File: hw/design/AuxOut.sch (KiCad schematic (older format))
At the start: 41 parts

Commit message: aux output, documentation
finished aux output circuit, updated a lot of documentation, added datasheets
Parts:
- added TP?: GND, TestPoint:TestPoint_Keystone_5000-5004_Miniature, symbol Connector:TestPoint
- added TP? (x3): AUX_G, TestPoint:TestPoint_Keystone_5000-5004_Miniature, symbol Connector:TestPoint
- C?: VRating 50V -> 16V
- D?: value D_Schottky -> B130LAW-7-F; IRating (none) -> 1A; MfrNum (none) -> DiodesInc_B130LAW-7-F; VRating (none) -> 30V
- D?: footprint (none) -> Diode_SMD:D_SOD-123
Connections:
- net GND: now also TP?.1
- net GND1: now also TR?.6, TP?.1, TP?.1, TP?.1; no longer TR?.4
- net Fly_EN: now reaches R?.1, R?.2, U?.1 (EN/UVLO)
- net at D?.2 (A): now also TR?.4; no longer TR?.6
- net AuxIn renamed Vbus
- net AuxPOut renamed AuxOut_I
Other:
- moved on the sheet: C?, D?, R?, TP?

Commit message: reworked adjusters
new V/I adjustment scheme; modified LDO circuit to match
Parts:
- added C?: 4.7u, Capacitor_SMD:C_1206_3216Metric, symbol Device:C
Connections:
- net AuxOut_I: now also C?.1
- net GND1: now also C?.2
- no-connect marks 1 -> 2
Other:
- note added: "All resistors 0603 size unless otherwise stated\nAll capacitors 0603 size unless otherwise stated\nAll capacitors rated for 16V unless otherwise stated"
- note added: "Aux Output Indicator\n(Optional Circuit)"
- note removed: "Aux Output Indicator"
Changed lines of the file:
@@
 Connection ~ 9500 1850
 Wire Wire Line
-	9500 1850 9800 1850
+	9500 1850 10000 1850
 $Comp
 L power:GND1 #PWR?
@@
 Text Notes 6900 5450 0    50   ~ 0
 Slow On\nFast Off
-Text Notes 7200 3950 0    100  ~ 0
-Aux Output Indicator
+Text Notes 7050 3900 0    100  ~ 0
+Aux Output Indicator\n(Optional Circuit)
 Text Notes 10000 3000 0    50   ~ 0
 Triggers at 4.75V
@@
 Text Label 2650 2400 0    50   ~ 0
 Fly_EN
-Text HLabel 9800 1850 2    50   BiDi ~ 0
+Text HLabel 10350 1850 2    50   BiDi ~ 0
 AuxOut_I
 Text HLabel 1650 1700 0    50   BiDi ~ 0
@@
 	1    0    0    1
 $EndComp
+NoConn ~ 4550 2000
+$Comp
+L Device:C C?
+U 1 1 6038857F
+P 10000 2100
+F 0 "C?" H 10115 2191 50  0000 L CNN
+F 1 "4.7u" H 10115 2100 50  0000 L CNN
+F 2 "Capacitor_SMD:C_1206_3216Metric" H 10038 1950 50  0001 C CNN
+F 3 "~" H 10000 2100 50  0001 C CNN
+F 4 "Murata_GRM21BR71C475KE51L" H 10000 2100 50  0001 C CNN "MfrNum"
+F 5 "16V" H 10115 2055 50  0001 L CNN "VRating"
+F 6 "0805" H 10115 2009 50  0000 L CNN "Size"
+	1    10000 2100
+	1    0    0    -1
+$EndComp
+Wire Wire Line
+	10000 1950 10000 1850
+Connection ~ 10000 1850
+Wire Wire Line
+	10000 1850 10350 1850
+$Comp
+L power:GND1 #PWR?
+U 1 1 6038EEFA
+P 10000 2350
+F 0 "#PWR?" H 10000 2100 50  0001 C CNN
+F 1 "GND1" H 10005 2177 50  0000 C CNN
+F 2 "" H 10000 2350 50  0001 C CNN
+F 3 "" H 10000 2350 50  0001 C CNN
+	1    10000 2350
+	1    0    0    -1
+$EndComp
+Wire Wire Line
+	10000 2350 10000 2250
+Text Notes 700  7600 0    50   ~ 0
+All resistors 0603 size unless otherwise stated\nAll capacitors 0603 size unless otherwise stated\nAll capacitors rated for 16V unless otherwise stated
 $EndSCHEMATC

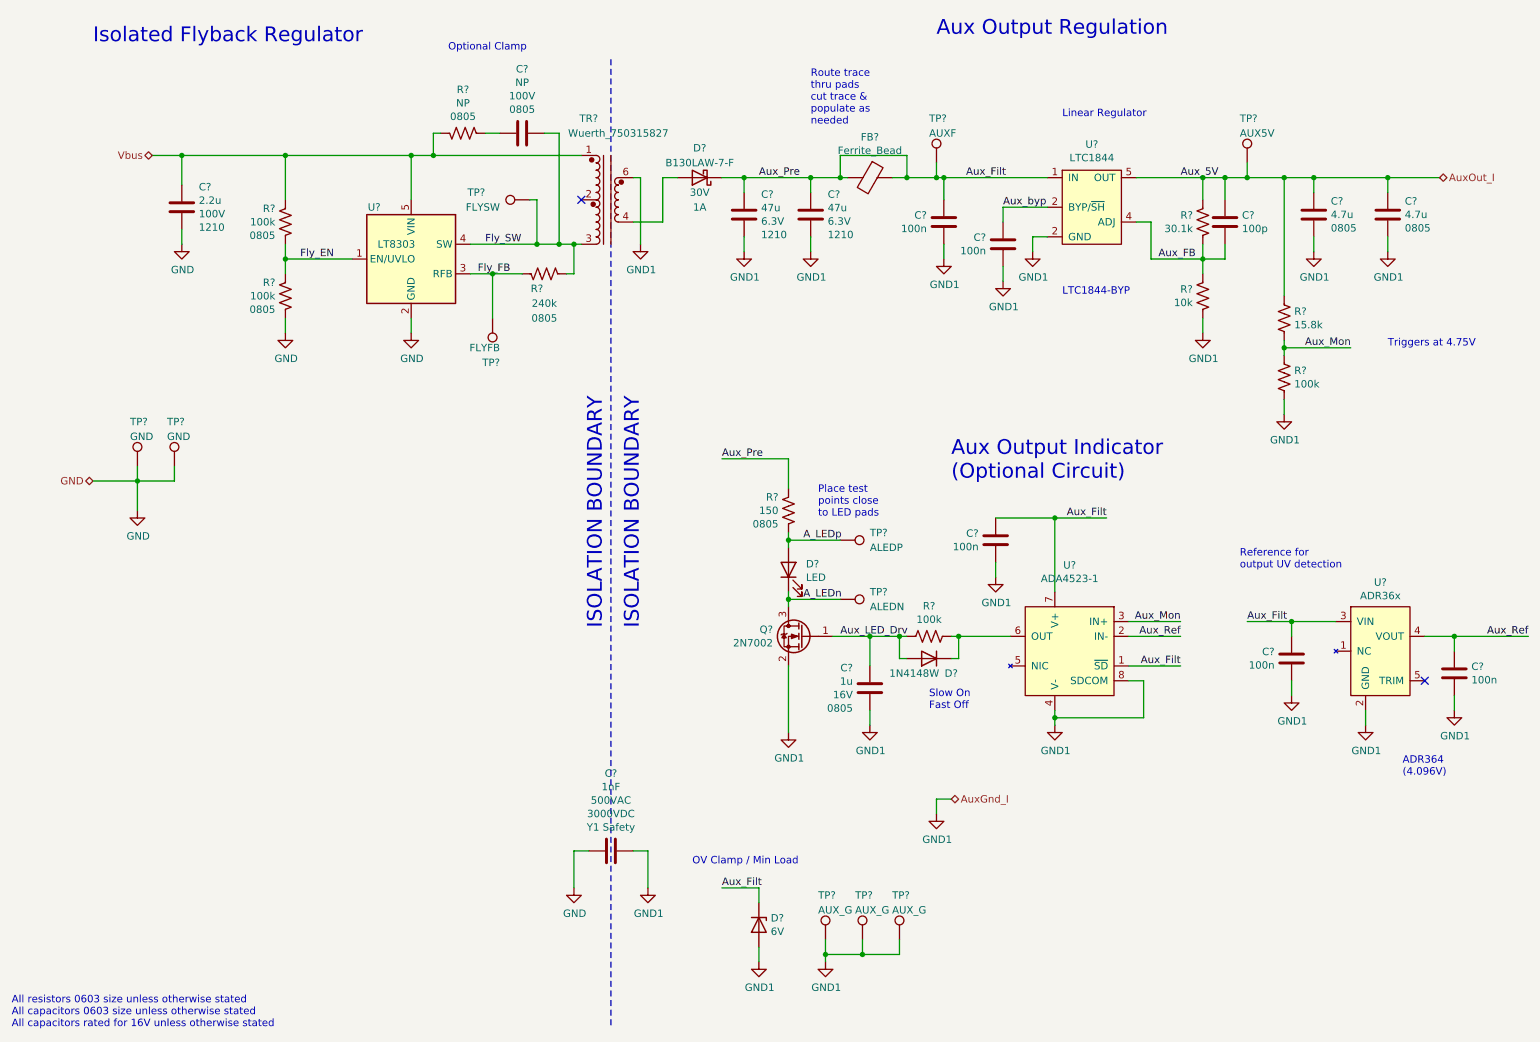
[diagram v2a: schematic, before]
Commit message: label/net reorg, primary SW starting
some reorganization of top-level naming for nets and hierarchical pins

fixed a few part selection issues

started on primary switcher sheet
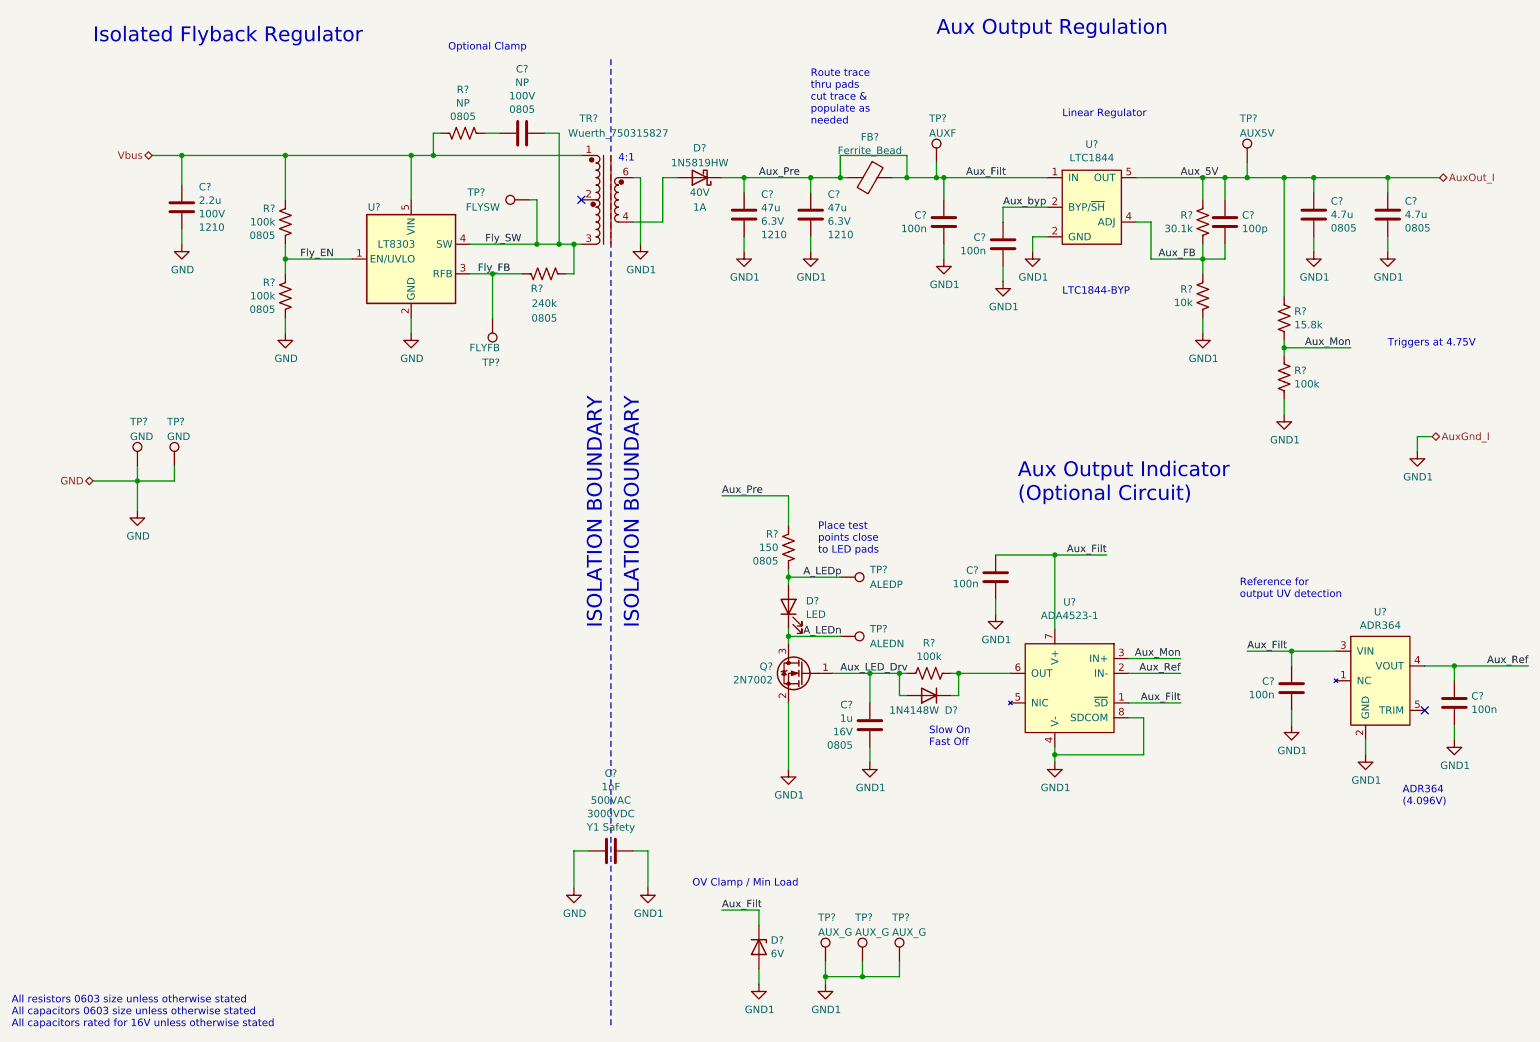
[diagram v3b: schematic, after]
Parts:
- D?: value B130LAW-7-F -> 1N5819HW; MfrNum DiodesInc_B130LAW-7-F -> DiodesInc_1N5819HW-7-F; VRating 30V -> 40V
- U?: value ADR36x -> ADR364
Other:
- note added: "4:1"
- moved on the sheet: C?, D?, Q?, R?, TP?, U?

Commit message: sims, new devices, code started
made some simulations & calculations, started working on code (moved devices into individual header files), new devices chosen in library
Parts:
- added TP?: Vbus, TestPoint:TestPoint_Keystone_5000-5004_Miniature, symbol Connector:TestPoint
- D?: value 1N5819HW -> PMEG2005EGW; IRating 1A -> 0.5A; MfrNum DiodesInc_1N5819HW-7-F -> Nexperia_PMEG2005EGW; VRating 40V -> 20V
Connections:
- net Vbus: now also TP?.1
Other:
- note added: "Lower-voltage\nfootprint-compatile\npart : LT3001"
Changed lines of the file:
@@
 P 5350 1850
 F 0 "D?" H 5350 1650 50  0000 C CNN
-F 1 "1N5819HW" H 5350 1750 50  0000 C CNN
+F 1 "PMEG2005EGW" H 5350 1750 50  0000 C CNN
 F 2 "Diode_SMD:D_SOD-123" H 5350 1850 50  0001 C CNN
 F 3 "~" H 5350 1850 50  0001 C CNN
-F 4 "DiodesInc_1N5819HW-7-F" H 5350 1850 50  0001 C CNN "MfrNum"
-F 5 "40V" H 5350 1950 50  0000 C CNN "VRating"
-F 6 "1A" H 5350 2050 50  0000 C CNN "IRating"
+F 4 "Nexperia_PMEG2005EGW" H 5350 1850 50  0001 C CNN "MfrNum"
+F 5 "20V" H 5350 1950 50  0000 C CNN "VRating"
+F 6 "0.5A" H 5350 2050 50  0000 C CNN "IRating"
 	1    5350 1850
 	-1   0    0    1
@@
 Connection ~ 2550 1700
 Wire Wire Line
-	2550 1700 3400 1700
+	2550 1700 2750 1700
 $Comp
 L power:GND #PWR?
@@
 Text Notes 4800 1750 0    50   ~ 0
 4:1
+$Comp
+L Connector:TestPoint TP?
+U 1 1 6068DAC6
+P 2750 1550
+AR Path="/5E80D1C0/6068DAC6" Ref="TP?"  Part="1"
+AR Path="/5E80D210/6068DAC6" Ref="TP?"  Part="1"
+AR Path="/5E84FADE/6068DAC6" Ref="TP?"  Part="1"
+AR Path="/5ECFB146/6068DAC6" Ref="TP?"  Part="1"
+AR Path="/5EB6CA11/6068DAC6" Ref="TP?"  Part="1"
+F 0 "TP?" H 2700 1850 50  0000 L CNN
+F 1 "Vbus" H 2700 1750 50  0000 L CNN
+F 2 "TestPoint:TestPoint_Keystone_5000-5004_Miniature" H 2950 1550 50  0001 C CNN
+F 3 "~" H 2950 1550 50  0001 C CNN
+	1    2750 1550
+	1    0    0    -1
+$EndComp
+Wire Wire Line
+	2750 1550 2750 1700
+Connection ~ 2750 1700
+Wire Wire Line
+	2750 1700 3400 1700
+Text Notes 2850 3500 0    50   ~ 0
+Lower-voltage\nfootprint-compatile\npart : LT3001
 $EndSCHEMATC
